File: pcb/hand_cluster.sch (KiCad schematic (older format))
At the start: 55 parts, among them U1 ProMicro

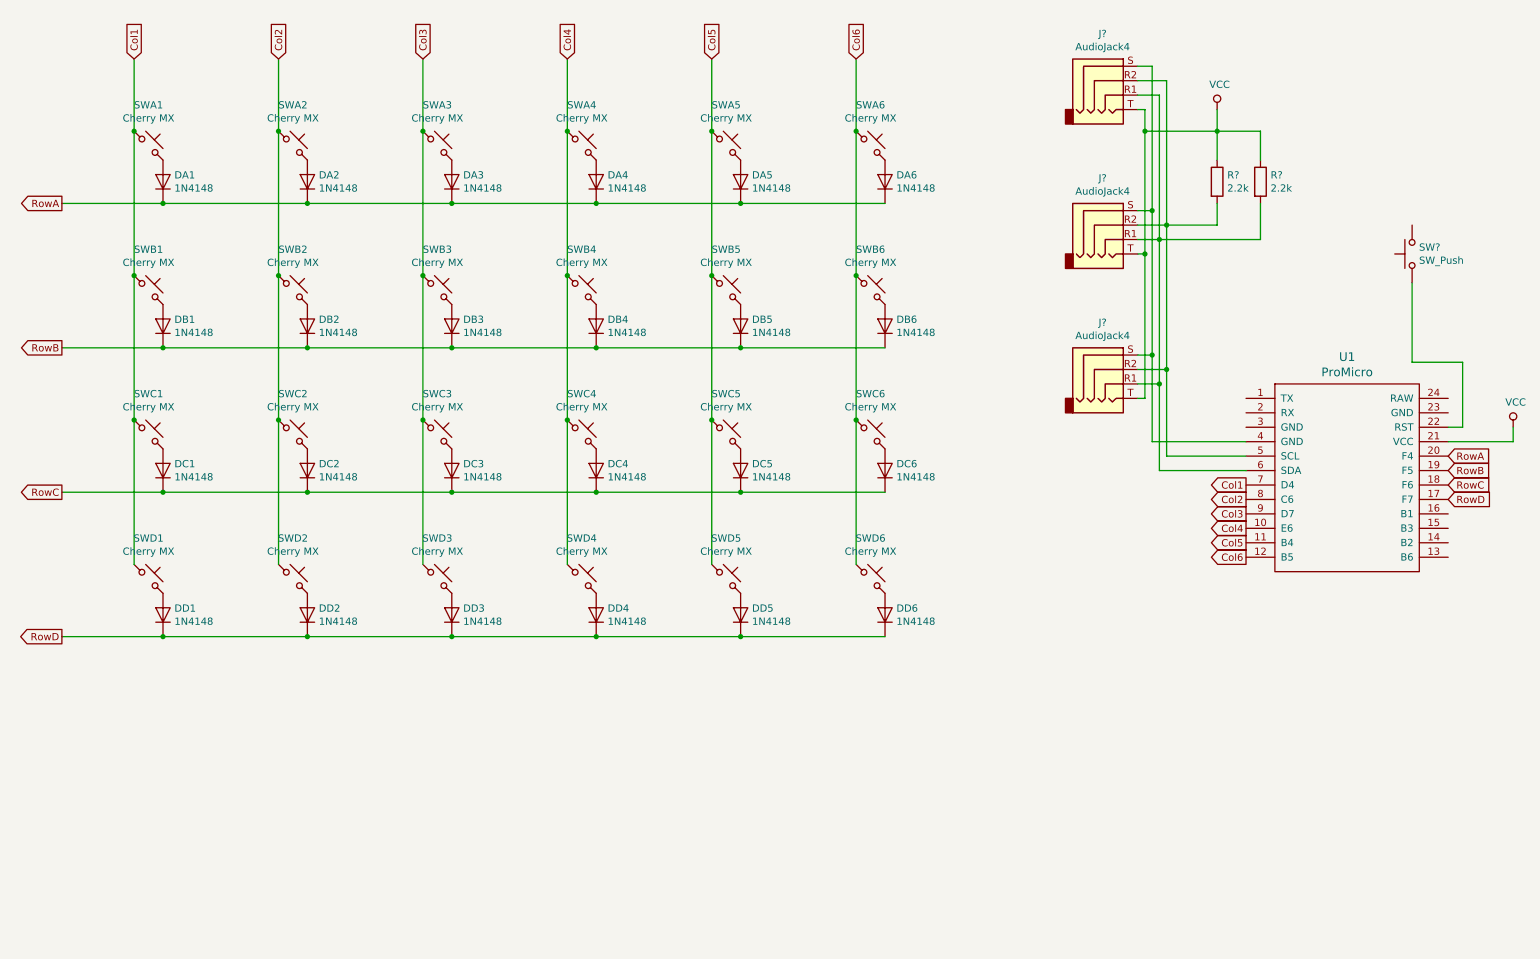
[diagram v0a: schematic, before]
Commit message: Renamed pcb files, added two encoders to schematics
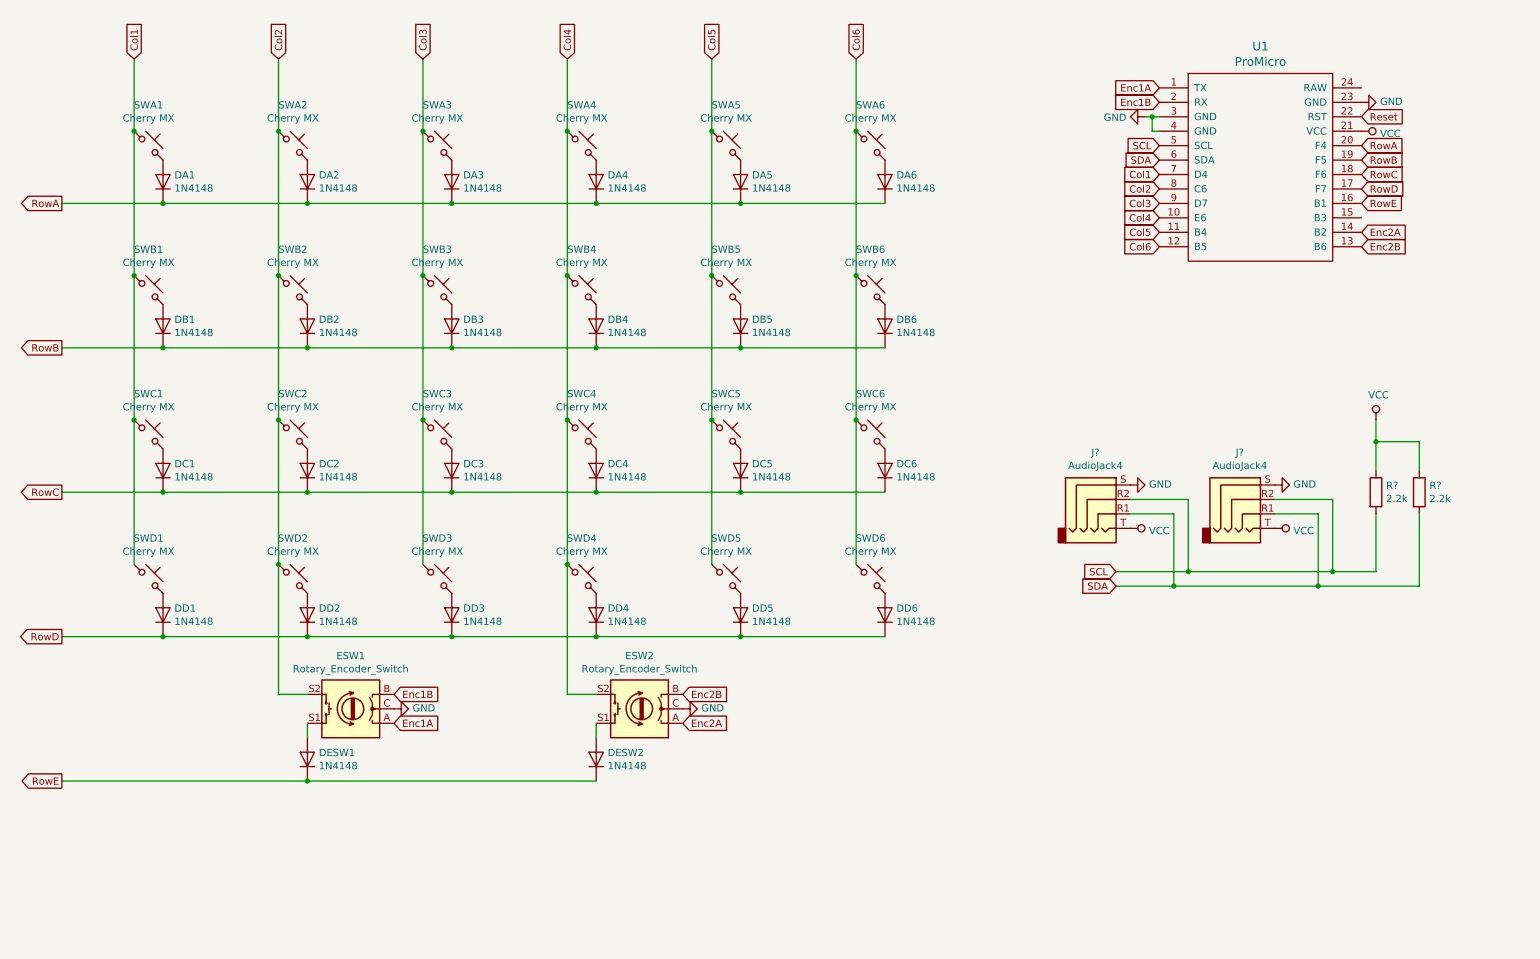
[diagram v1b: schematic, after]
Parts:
- removed J? (x3): AudioJack4, symbol Connector:AudioJack4
- removed R? (x2): 2.2k, symbol Device:R
- removed SW?: SW_Push, symbol Switch:SW_Push
- added DESW1, DESW2: 1N4148, Diode_THT:D_DO-35_SOD27_P7.62mm_Horizontal, symbol Diode:1N4148
- added ESW1, ESW2: Rotary_Encoder_Switch, symbol Device:Rotary_Encoder_Switch
- added J? (x2): AudioJack4, symbol Connector:AudioJack4
- added R? (x2): 2.2k, symbol Device:R
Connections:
- net Col2: now also ESW1.S2
- net Col4: now also ESW2.S2
- net VCC: now also J?.T, J?.T, R?.1, R?.1
- net Enc1A: now reaches U1.1 (TX)
- net Enc1A: now also ESW1.A
- net Enc2B: now reaches U1.13 (B6)
- net Enc2B: now also ESW2.B
- net Enc2A: now reaches U1.14 (B2)
- net Enc2A: now also ESW2.A
- net RowE: now reaches U1.16 (B1)
- net RowE: now also DESW1.1 (K), DESW2.1 (K)
- net Enc1B: now reaches U1.2 (RX)
- net Enc1B: now also ESW1.B
- net Reset: now reaches U1.22 (RST)
- net GND: now reaches U1.23 (GND)
- net GND: now also U1.3 (GND), U1.4 (GND), ESW1.C, ESW2.C, J?.S, J?.S
- net SCL: now reaches U1.5 (SCL)
- net SCL: now also J?.R2, J?.R2, R?.2
- net SDA: now reaches U1.6 (SDA)
- net SDA: now also J?.R1, J?.R1, R?.2
- new net: DESW2.2 (A), ESW2.S1
- new net: DESW1.2 (A), ESW1.S1
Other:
- moved on the sheet: U1

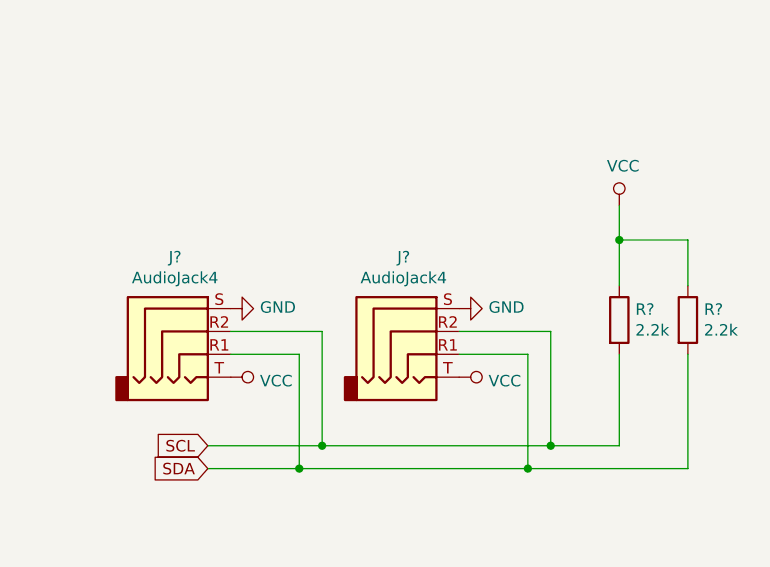
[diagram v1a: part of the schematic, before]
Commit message: Linked components with pcb footprints
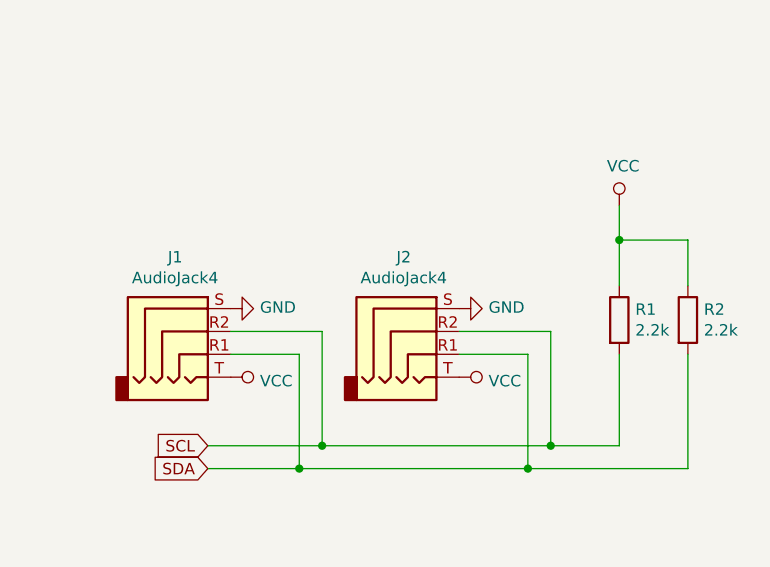
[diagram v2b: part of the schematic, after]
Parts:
- ESW1, ESW2: footprint (none) -> Keebio-Parts:RotaryEncoder_EC11
- J1, J2: renamed from J?; footprint (none) -> Keebio-Parts:TRRS-PJ-320A-dual
- R1, R2: renamed from R?; footprint (none) -> Keebio-Parts:Resistor
- SWA1, SWA2, SWA3, SWA4, SWA5, SWA6, SWB1, SWB2, SWB3, SWB4, SWB5, SWB6, SWC1, SWC2, SWC3, SWC4, SWC5, SWC6, SWD1, SWD2, SWD3, SWD4, SWD5, SWD6: footprint keyboard_parts:Kailh_MX_Socket -> Keebio-Parts:Hybrid_PCB_100H_Dual_hole-nosilk
- U1: footprint promicro:ProMicro -> Keebio-Parts:ArduinoProMicro-Mini-USB

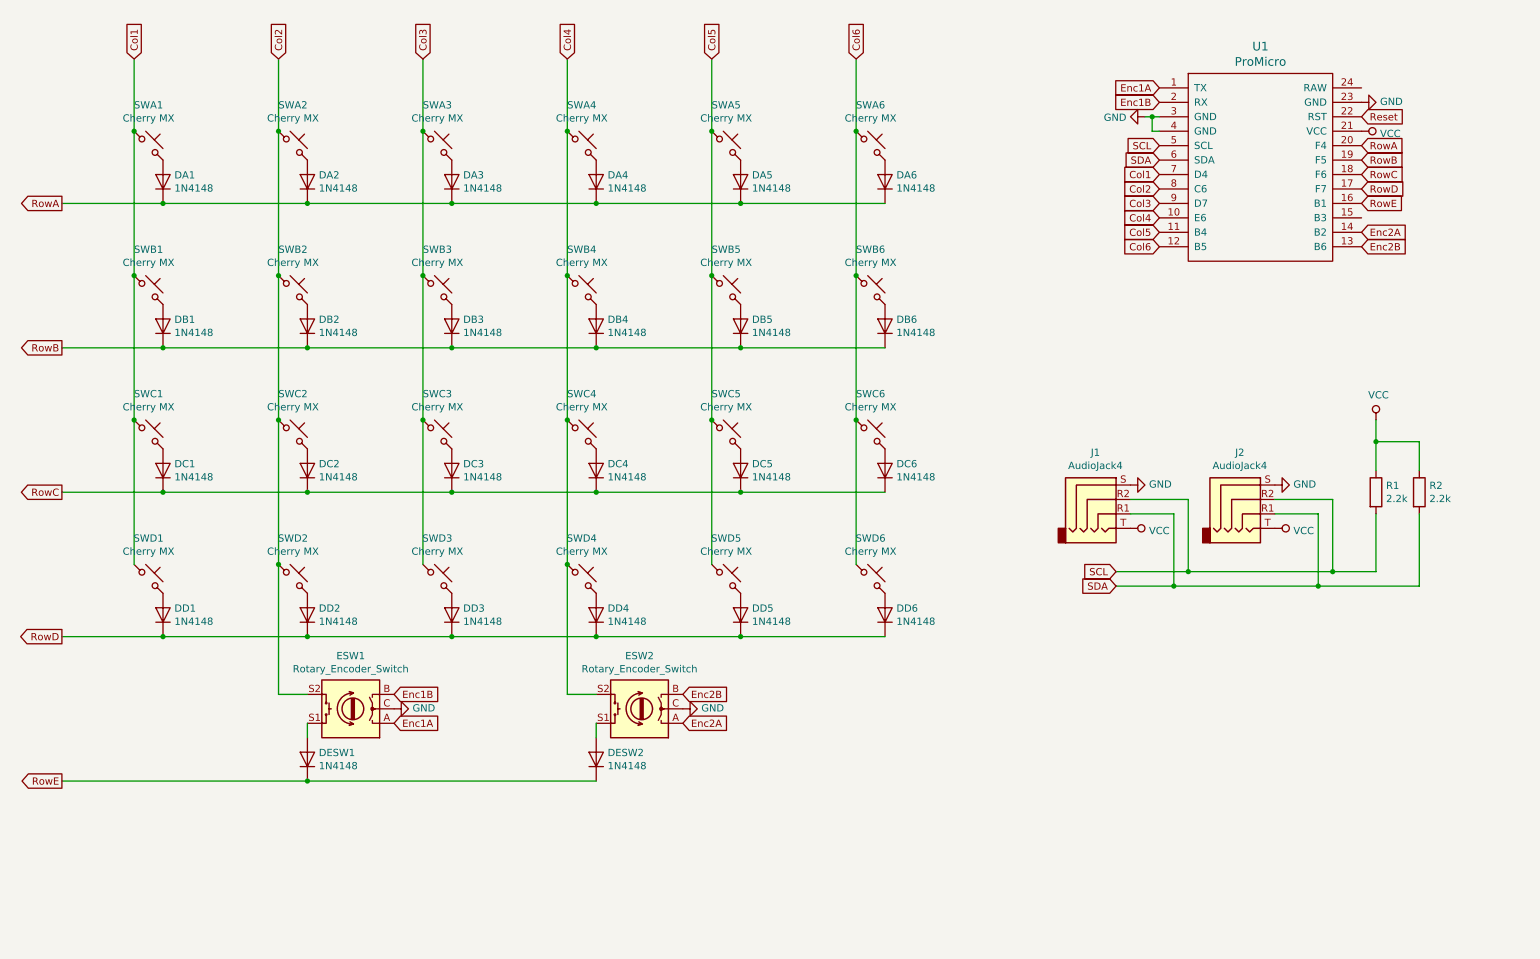
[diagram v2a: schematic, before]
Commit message: Designed the version of a plaid modular hand cluster
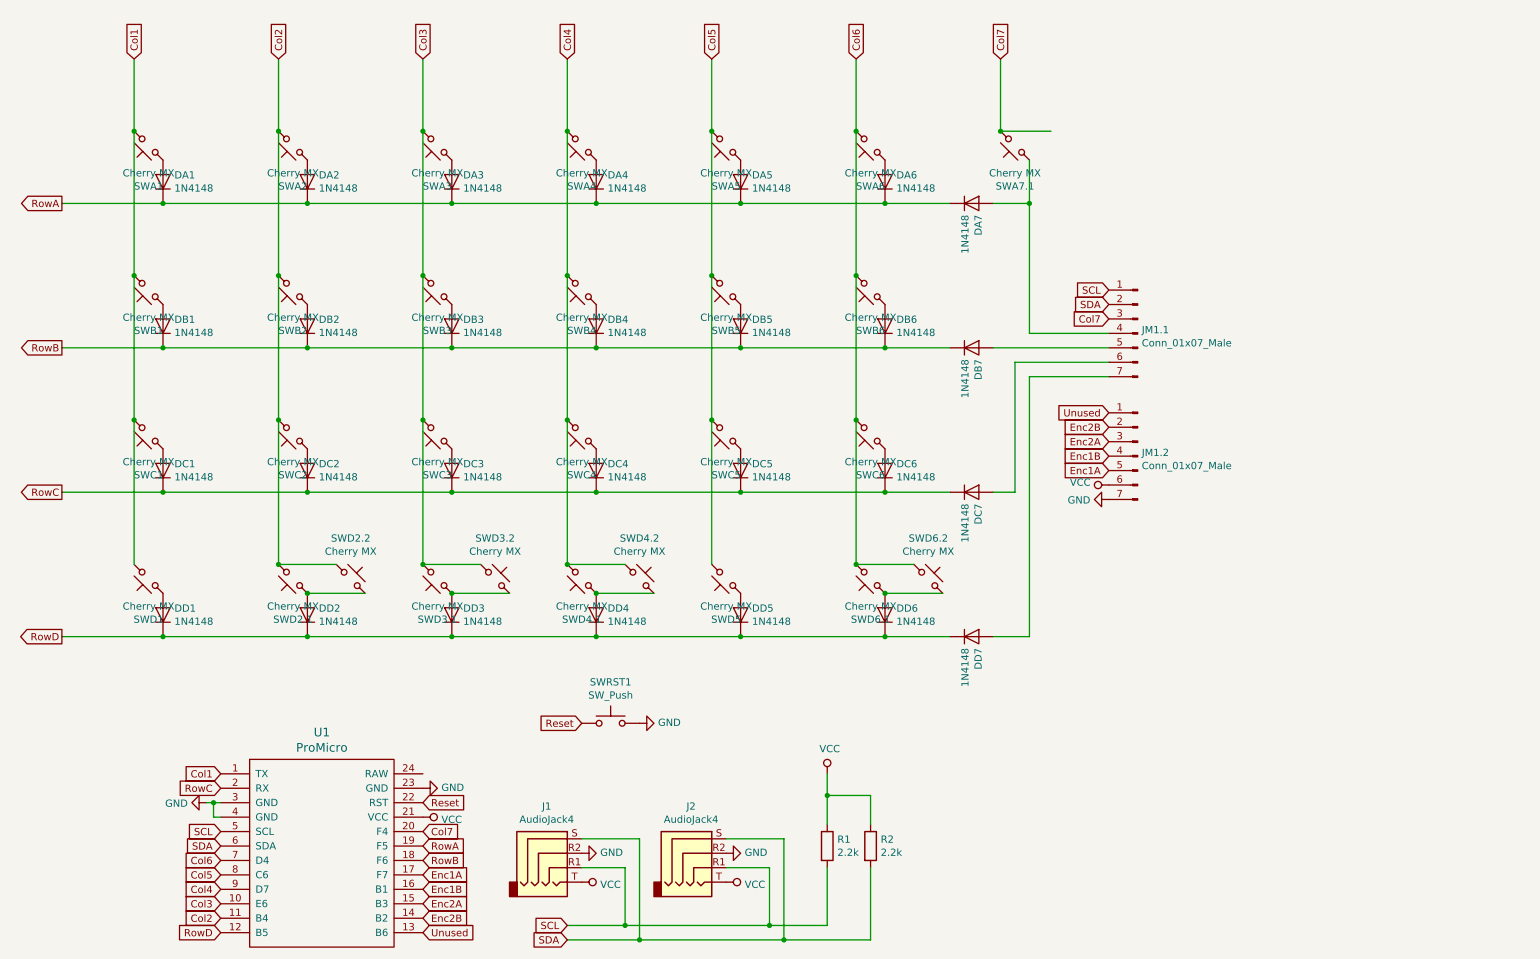
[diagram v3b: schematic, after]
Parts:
- removed ESW1, ESW2: Rotary_Encoder_Switch, Keebio-Parts:RotaryEncoder_EC11, symbol Device:Rotary_Encoder_Switch
- removed SWD6: Cherry MX, Keebio-Parts:Hybrid_PCB_100H_Dual_hole-nosilk, symbol Switch:SW_Push_45deg
- added DA7, DB7: 1N4148, Diode_THT:D_DO-35_SOD27_P7.62mm_Horizontal, symbol Diode:1N4148
- added JM1.1, JM1.2: Conn_01x07_Male, Connector_PinHeader_2.54mm:PinHeader_1x07_P2.54mm_Vertical, symbol Connector:Conn_01x07_Male
- added SWA7.1, SWD2.2, SWD3.2, SWD4.2, SWD6.1, SWD6.2: Cherry MX, Keebio-Parts:Hybrid_Plate_100H_Dual_hole-nosilk, symbol Switch:SW_Push_45deg
- added SWRST1: SW_Push, Button_Switch_THT:SW_PUSH_6mm, symbol Switch:SW_Push
- J1, J2: footprint Keebio-Parts:TRRS-PJ-320A-dual -> Keebio-Parts:TRRS-PJ-320A-dual-labeled
- SWA1, SWB1, SWC1, SWD1: footprint Keebio-Parts:Hybrid_PCB_100H_Dual_hole-nosilk -> acerne:Hybrid_Plate_150H_Dual_hole-nosilk
- SWA2, SWA3, SWA4, SWA5, SWA6, SWB2, SWB3, SWB4, SWB5, SWB6, SWC2, SWC3, SWC4, SWC5, SWC6, SWD5: footprint Keebio-Parts:Hybrid_PCB_100H_Dual_hole-nosilk -> Keebio-Parts:Hybrid_Plate_100H_Dual_hole-nosilk
- SWD2.1: renamed from SWD2; footprint Keebio-Parts:Hybrid_PCB_100H_Dual_hole-nosilk -> Keebio-Parts:Hybrid_Plate_100H_Dual_hole-nosilk
- SWD3.1: renamed from SWD3; footprint Keebio-Parts:Hybrid_PCB_100H_Dual_hole-nosilk -> Keebio-Parts:Hybrid_Plate_100H_Dual_hole-nosilk
- SWD4.1: renamed from SWD4; footprint Keebio-Parts:Hybrid_PCB_100H_Dual_hole-nosilk -> Keebio-Parts:Hybrid_Plate_100H_Dual_hole-nosilk
- U1: footprint Keebio-Parts:ArduinoProMicro-Mini-USB -> Keebio-Parts:ArduinoProMicro
- renumbered DESW2 to DC7, DESW1 to DD7
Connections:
- net Col1: now also SWA1.2, SWB1.2, SWC1.2, SWD1.2, U1.1 (TX); no longer SWA1.1, SWB1.1, SWC1.1, SWD1.1, U1.7 (D4)
- net Col2: now also SWA2.2, SWB2.2, SWC2.2, SWD2.1.2, U1.11 (B4), SWD2.2.1; no longer SWA2.1, SWB2.1, SWC2.1, SWD2.1.1, U1.8 (C6)
- net Col3: now also SWA3.2, SWB3.2, SWC3.2, SWD3.1.2, U1.10 (E6), SWD3.2.1; no longer SWA3.1, SWB3.1, SWC3.1, SWD3.1.1, U1.9 (D7)
- net Col4: now also SWA4.2, SWB4.2, SWC4.2, SWD4.1.2, U1.9 (D7), SWD4.2.1; no longer SWA4.1, SWB4.1, SWC4.1, SWD4.1.1, U1.10 (E6)
- net Col5: now also SWA5.2, SWB5.2, SWC5.2, SWD5.2, U1.8 (C6); no longer SWA5.1, SWB5.1, SWC5.1, SWD5.1, U1.11 (B4)
- net Col6: now also SWA6.2, SWB6.2, SWC6.2, U1.7 (D4), SWD6.1.2, SWD6.2.1; no longer SWA6.1, SWB6.1, SWC6.1, U1.12 (B5)
- net Enc1A: now also U1.17 (F7), JM1.2.5 (Pin_5); no longer U1.1 (TX)
- net Enc1B: now also U1.16 (B1), JM1.2.4 (Pin_4); no longer U1.2 (RX)
- net Enc2A: now also U1.15 (B3), JM1.2.3 (Pin_3); no longer U1.14 (B2)
- net Enc2B: now also U1.14 (B2), JM1.2.2 (Pin_2); no longer U1.13 (B6)
- net GND: now also J1.R2, J2.R2, JM1.2.7 (Pin_7), SWRST1.2; no longer J1.S, J2.S
- net Reset: now also SWRST1.1
- net RowA: now also U1.19 (F5), DA7.1 (K); no longer U1.20 (F4)
- net RowB: now also U1.18 (F6), DB7.1 (K); no longer U1.19 (F5)
- net RowC: now also DC7.1 (K), U1.2 (RX); no longer U1.18 (F6)
- net RowD: now also DD7.1 (K), U1.12 (B5); no longer U1.17 (F7)
- net SCL: now also J1.R1, J2.R1, JM1.1.1 (Pin_1); no longer J1.R2, J2.R2
- net SDA: now also J1.S, J2.S, JM1.1.2 (Pin_2); no longer J1.R1, J2.R1
- net VCC: now also JM1.2.6 (Pin_6)
- net at DA1.2 (A): now also SWA1.1; no longer SWA1.2
- net at DA2.2 (A): now also SWA2.1; no longer SWA2.2
- net at DA3.2 (A): now also SWA3.1; no longer SWA3.2
- net at DA4.2 (A): now also SWA4.1; no longer SWA4.2
- net at DA5.2 (A): now also SWA5.1; no longer SWA5.2
- net at DA6.2 (A): now also SWA6.1; no longer SWA6.2
- net at DB1.2 (A): now also SWB1.1; no longer SWB1.2
- net at DB2.2 (A): now also SWB2.1; no longer SWB2.2
- net at DB3.2 (A): now also SWB3.1; no longer SWB3.2
- net at DB4.2 (A): now also SWB4.1; no longer SWB4.2
- net at DB5.2 (A): now also SWB5.1; no longer SWB5.2
- net at DB6.2 (A): now also SWB6.1; no longer SWB6.2
- net at DC1.2 (A): now also SWC1.1; no longer SWC1.2
- net at DC2.2 (A): now also SWC2.1; no longer SWC2.2
- net at DC3.2 (A): now also SWC3.1; no longer SWC3.2
- net at DC4.2 (A): now also SWC4.1; no longer SWC4.2
- net at DC5.2 (A): now also SWC5.1; no longer SWC5.2
- net at DC6.2 (A): now also SWC6.1; no longer SWC6.2
- net at DD1.2 (A): now also SWD1.1; no longer SWD1.2
- net at DD2.2 (A): now also SWD2.1.1, SWD2.2.2; no longer SWD2.1.2
- net at DD3.2 (A): now also SWD3.1.1, SWD3.2.2; no longer SWD3.1.2
- net at DD4.2 (A): now also SWD4.1.1, SWD4.2.2; no longer SWD4.1.2
- net at DD5.2 (A): now also SWD5.1; no longer SWD5.2
- net at DD6.2 (A): now also SWD6.1.1, SWD6.2.2
- net at DC7.2 (A): now also JM1.1.6 (Pin_6)
- net at DD7.2 (A): now also JM1.1.7 (Pin_7)
- removed net RowE: DC7.1 (K), DD7.1 (K), U1.16 (B1)
- new net: DA7.2 (A), JM1.1.4 (Pin_4), SWA7.1.1
- new net: DB7.2 (A), JM1.1.5 (Pin_5)
- new net Col7: JM1.1.3 (Pin_3), SWA7.1.2, U1.20 (F4)
- new net Unused: JM1.2.1 (Pin_1), U1.13 (B6)
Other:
- moved on the sheet: DC7, DD7, J1, J2, R1, R2, U1
